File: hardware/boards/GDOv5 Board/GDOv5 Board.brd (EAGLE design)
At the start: 34 x 78.7 mm, 32 parts, among them IC1 DS1820, IC2 3.3V REG, J1 DCJ0202

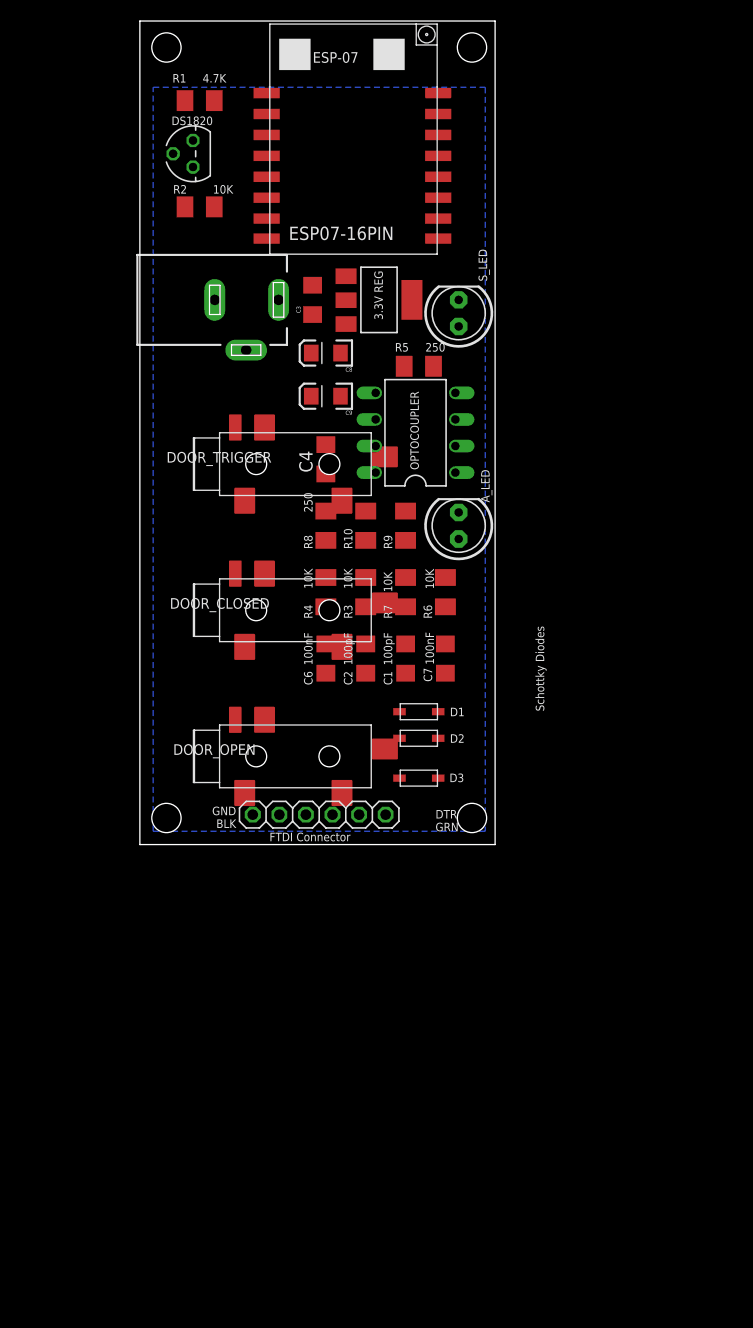
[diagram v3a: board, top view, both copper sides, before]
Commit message: Redesigning main board for more SMT components
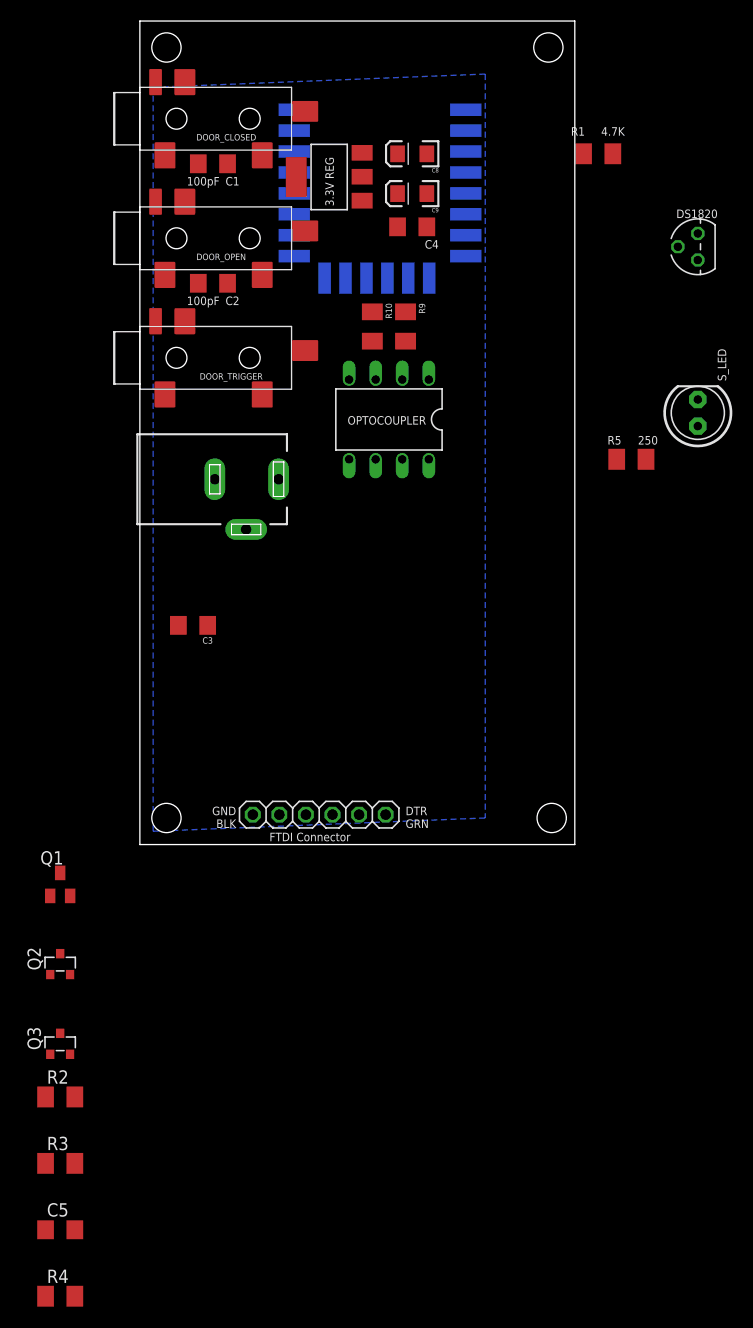
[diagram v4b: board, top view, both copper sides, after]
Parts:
- removed A_LED: (no value), adafruit:LED5MM
- removed C6, C7: 100nF, resistor:C1206
- removed D1: Schottky Diodes, adafruit:SOD-123
- removed D2, D3: (no value), adafruit:SOD-123
- removed R6, R7: 10K, resistor:M3216
- removed R8: 250, resistor:M3216
- added C5: 100nF, resistor:C1206
- added Q1: BSS84, transistor-small-signal:SOT23
- added Q2, Q3: BSS138, bss138_10:SOT23
- R2, R3: value 10K -> 100k
- R4: value 10K -> 50
- U$1: value ESP07-16PIN -> (none); device esp8266modules:ESP07-16PIN -> esp8266modules:ESP12E-SMD
- moved R2 86.1 mm to (-7.62, -22.9)
- moved R4 71.9 mm to (-7.62, -41.9), turned to 0 degrees
- moved R3 61.9 mm to (-7.62, -29.2), turned to 0 degrees
- moved C1 50.8 mm to (6.99, 66.4), turned to 180 degrees
- moved DOOR_OPEN 50.1 mm to (0.00, 62.2)
- moved IC1 49.1 mm to (53.3, 58.4)
- moved DOOR_CLOSED 47.6 mm to (0.00, 73.7)
- moved C2 38.7 mm to (6.99, 54.9), turned to 180 degrees
- moved R1 38.4 mm to (43.8, 67.3)
- moved C3 33.1 mm to (5.08, 22.2), turned to 180 degrees
- moved S_LED 24.8 mm to (53.3, 42.5)
- moved C4 23.7 mm to (26.0, 60.3), turned to 180 degrees
- moved R5 22.2 mm to (47.0, 38.1)
- moved C9 21.1 mm to (26.0, 63.5)
- moved C8 20.8 mm to (26.0, 67.3)
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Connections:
- removed net N$5: A_LED.K, R8.1
- removed net RXD_5V: D1.C, JP1.3
- new net DTR: JP1.1, Q1.1, R2.2
- net +3.3V: now also Q1.2; no longer R4.1, R6.2, R7.2
- net +5V: now also J1.3; no longer J1.1
- net ARD0_FLASH: now also Q2.3; no longer D3.A, R4.2, R6.1
- net ARD16: no longer A_LED.A
- net ENABLE: now also Q3.3; no longer C7.1, R2.2, R7.1
- net GND: now also J1.1, Q2.2, Q3.2, R4.1; no longer C6.2, J1.3, R8.2
- net N$1: now also C5.1, Q1.3, Q2.1, R3.2; no longer C7.2, D2.A, D3.C
- net N$2: now also C5.2, Q3.1, R4.2; no longer D2.C, JP1.1
- net RESET: now also U$1.RESET; no longer C6.1, R3.2, U$1.REST
- net RXD: now also JP1.3, U$1.RXD0; no longer D1.A, U$1.RX
- net TXD: now also U$1.TXD0; no longer U$1.TX
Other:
- board size 34 x 78.7 mm -> 41.6 x 78.7 mm

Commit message: Updating main board files
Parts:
- R4: value 50 -> 100k
- moved IC1 47.9 mm to (8.89, 76.2), turned to 0 degrees
- moved R1 31.3 mm to (14.0, 76.8), turned to 90 degrees
- moved S_LED 26.9 mm to (27.9, 33.7), turned to 180 degrees
- moved R5 25.7 mm to (21.6, 34.3)
- moved C3 21.1 mm to (7.30, 43.2), turned to 0 degrees
- moved CTRL_OUT 1.27 mm to (23.8, 43.2)
- moved R10 1.27 mm to (21.0, 50.8), turned to 0 degrees
- moved R9 1.27 mm to (26.7, 50.8), turned to 0 degrees
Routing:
- removed copper zone on layer 16, net GND

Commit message: Finalized version of board for OshPark
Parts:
- Q2, Q3: device bss138_10:SOT23 -> Ava:BSS138
- R10, R9: value 50 -> 50Ω
- moved R4 100.0 mm to (28.2, 51.4)
- moved C5 96.9 mm to (27.9, 54.6)
- moved R3 89.2 mm to (22.9, 54.6)
- moved Q3 84.7 mm to (26.7, 59.7)
- moved R2 81.5 mm to (17.8, 54.6)
- moved Q2 76.2 mm to (22.9, 59.7)
- moved Q1 67.7 mm to (19.1, 59.7)
- moved JP1 24.1 mm to (17.1, 28.3)
- moved C9 3.82 mm to (26.4, 67.3)
- moved C4 3.81 mm to (26.0, 64.1)
- moved C8 3.81 mm to (26.0, 71.1)
- moved R9 3.65 mm to (23.1, 51.4)
- moved C1 3.38 mm to (9.53, 64.1)
- moved R10 3.16 mm to (17.9, 51.4)
- moved S_LED 2.84 mm to (30.5, 34.9)
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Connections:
- net ARD0_FLASH: now also Q2.D; no longer Q2.3
- net ENABLE: now also Q3.D; no longer Q3.3
- net GND: now also Q2.S, Q3.S; no longer Q2.2, Q3.2
- net N$1: now also Q2.G; no longer Q2.1
- net N$2: now also Q3.G; no longer Q3.1
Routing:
- net TXD: track 0.00 -> 78.9 mm, vias 0 -> 1
- net +3.3V: track 0.00 -> 78.5 mm, vias 0 -> 1
- net RXD: track 0.00 -> 76.9 mm, vias 0 -> 2
- net +5V: track 0.00 -> 76.4 mm
- net GND: track 0.00 -> 74.1 mm, vias 0 -> 3
- net DTR: track 0.00 -> 48.9 mm
- net ARD14: track 0.00 -> 31.5 mm, vias 0 -> 1
- net ARD15: track 0.00 -> 30.8 mm, vias 0 -> 1
- net CTRL-: track 0.00 -> 29.5 mm
- net ARD02: track 0.00 -> 25.4 mm
- net DOOR+: track 0.00 -> 24.7 mm, vias 0 -> 1
- net ARD12: track 0.00 -> 20.4 mm
- net N$3: track 0.00 -> 19.1 mm
- net ARD0_FLASH: track 0.00 -> 17.4 mm, vias 0 -> 1
- net ARD13: track 0.00 -> 16.6 mm
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- added copper zone on layer 16, net GND
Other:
- board size 41.6 x 78.7 mm -> 34 x 53.6 mm

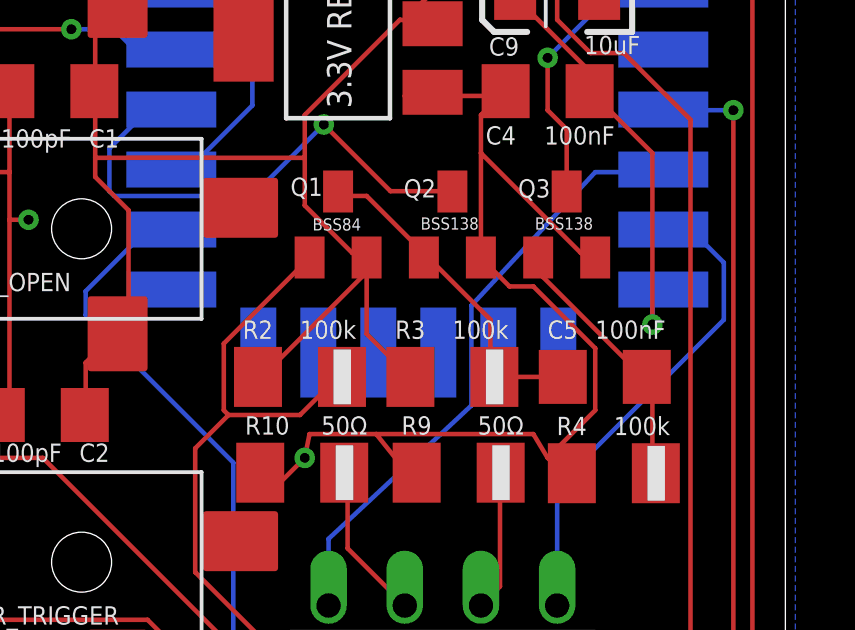
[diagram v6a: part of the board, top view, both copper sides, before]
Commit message: Fixing bad pull down connection in auto-reset circuit
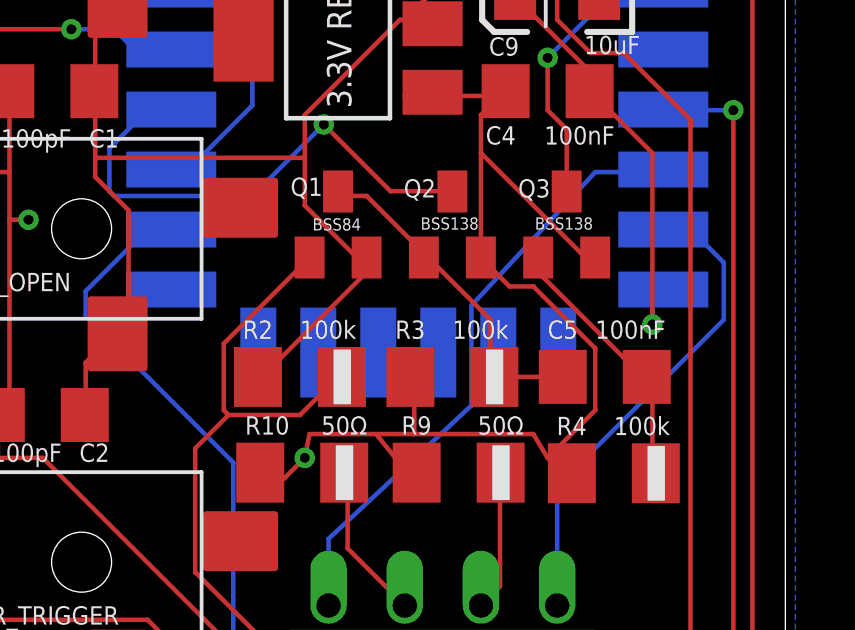
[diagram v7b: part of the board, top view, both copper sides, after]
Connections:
- net +3.3V: no longer R3.1
- net GND: now also R3.1
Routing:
- net +3.3V: track 78.5 -> 74.4 mm
- net GND: track 74.1 -> 76.2 mm

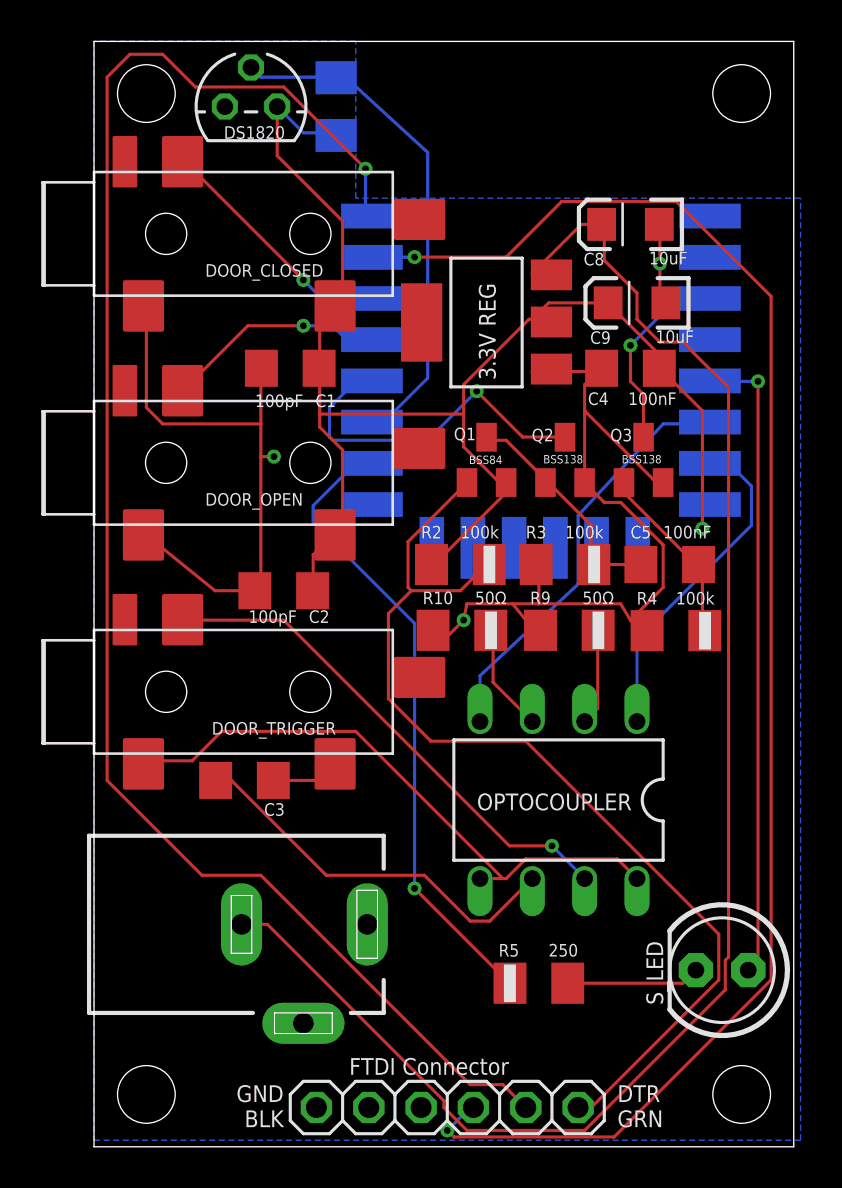
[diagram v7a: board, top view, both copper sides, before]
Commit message: Added pullup resistor for GPIO0
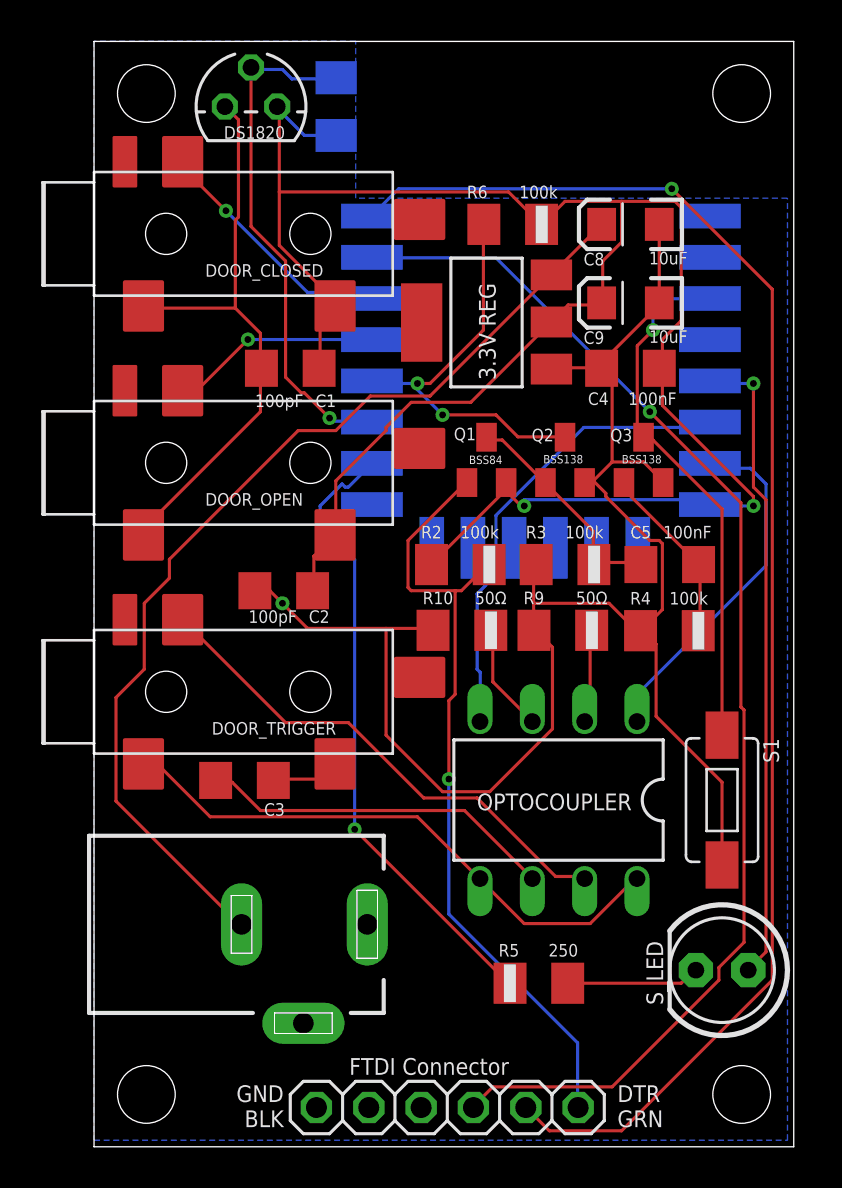
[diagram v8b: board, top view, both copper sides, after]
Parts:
- added R6: 100k, resistor:M3216
- added S1: RESET-SWITCH, SparkFun-Electromechanical:TACTILE-SWITCH-1101NE
- moved C9 0.32 mm to (26.0, 67.3)
- moved R4 0.32 mm to (27.9, 51.4)
- moved R9 0.32 mm to (22.8, 51.4)
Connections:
- net +3.3V: now also R6.2
- net ARD0_FLASH: now also R6.1
- net ENABLE: now also S1.P$1
- net GND: now also S1.P$2
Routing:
- net GND: track 76.2 -> 111.1 mm, vias 3 -> 1
- net +3.3V: track 74.4 -> 101.9 mm, vias 1 -> 2
- net +5V: track 76.4 -> 49.1 mm
- net ENABLE: track 9.50 -> 25.7 mm
- net RXD: track 76.9 -> 61.1 mm, vias 2 -> 1
- net DTR: track 48.9 -> 38.6 mm, vias 0 -> 1
- net TXD: track 78.9 -> 71.0 mm
- net ARD0_FLASH: track 17.4 -> 20.2 mm, vias 1 -> 2
- net ARD12: track 20.4 -> 22.8 mm
- net N$3: track 19.1 -> 17.4 mm
- net CTRL-: track 29.5 -> 28.1 mm
- net N$2: track 9.53 -> 8.75 mm
- net ARD13: track 16.6 -> 17.2 mm
- net ARD05: track 10.8 -> 10.2 mm
- net N$5: track 11.7 -> 11.2 mm
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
